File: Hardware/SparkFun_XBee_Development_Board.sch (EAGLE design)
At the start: 71 parts, among them J1 USB Female Type C Connector, J3 USB Female Type C Connector, J4 QWIIC_RIGHT_ANGLE, Q2 3.1A/30V/105mΩ, U1 FSUSB30MUX_MSOP10, U2 AP63203, U3 ESD Diode, U5 ESD Diode, U7 FT231XS

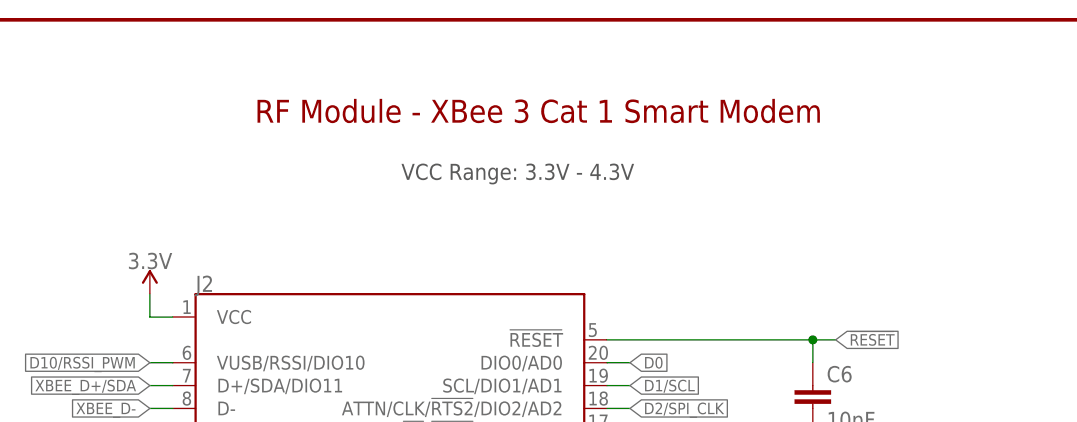
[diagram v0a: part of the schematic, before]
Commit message: Updates XBee section with correct name
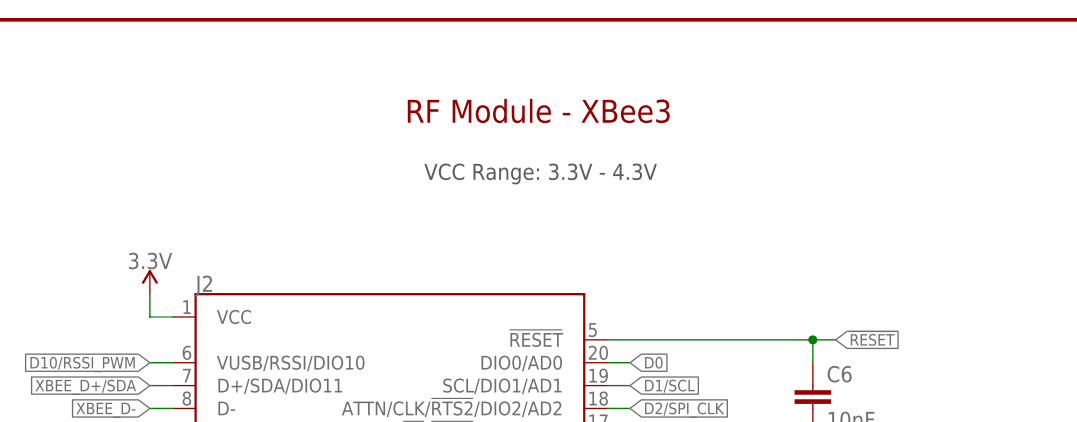
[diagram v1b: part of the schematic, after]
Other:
- note added: "RF Module - XBee3"
- note removed: "RF Module - XBee 3 Cat 1 Smart Modem"
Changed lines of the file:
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@@
 <sheet>
 <plain>
-<text x="45.72" y="261.62" size="1.778" layer="97" font="vector">VCC Range: 3.3V - 4.3V</text>
+<text x="48.26" y="261.62" size="1.778" layer="97" font="vector">VCC Range: 3.3V - 4.3V</text>
 <text x="363.22" y="269.24" size="2.54" layer="94" font="vector" align="center">USB to UART Bridge  - FT231XS</text>
 <text x="203.454" y="197.866" size="2.54" layer="94" font="vector" align="center">Buck Converter - AP63203</text>
@@
 <text x="172.72" y="96.52" size="1.778" layer="97" font="vector" align="center">Cut I2C jumper to remove pullups.</text>
 <text x="274.32" y="96.52" size="1.778" layer="97" font="vector" align="center">Cut respective jumper to sever power to LED.</text>
-<text x="60.96" y="269.24" size="2.54" layer="94" font="vector" align="center">RF Module - XBee 3 Cat 1 Smart Modem</text>
+<text x="60.96" y="269.24" size="2.54" layer="94" font="vector" align="center">RF Module - XBee3</text>
 <wire x1="0" y1="187.96" x2="121.92" y2="187.96" width="0.2032" layer="97" style="longdash"/>
 <text x="60.96" y="180.34" size="2.54" layer="94" font="vector" align="center">0.1" Headers</text>

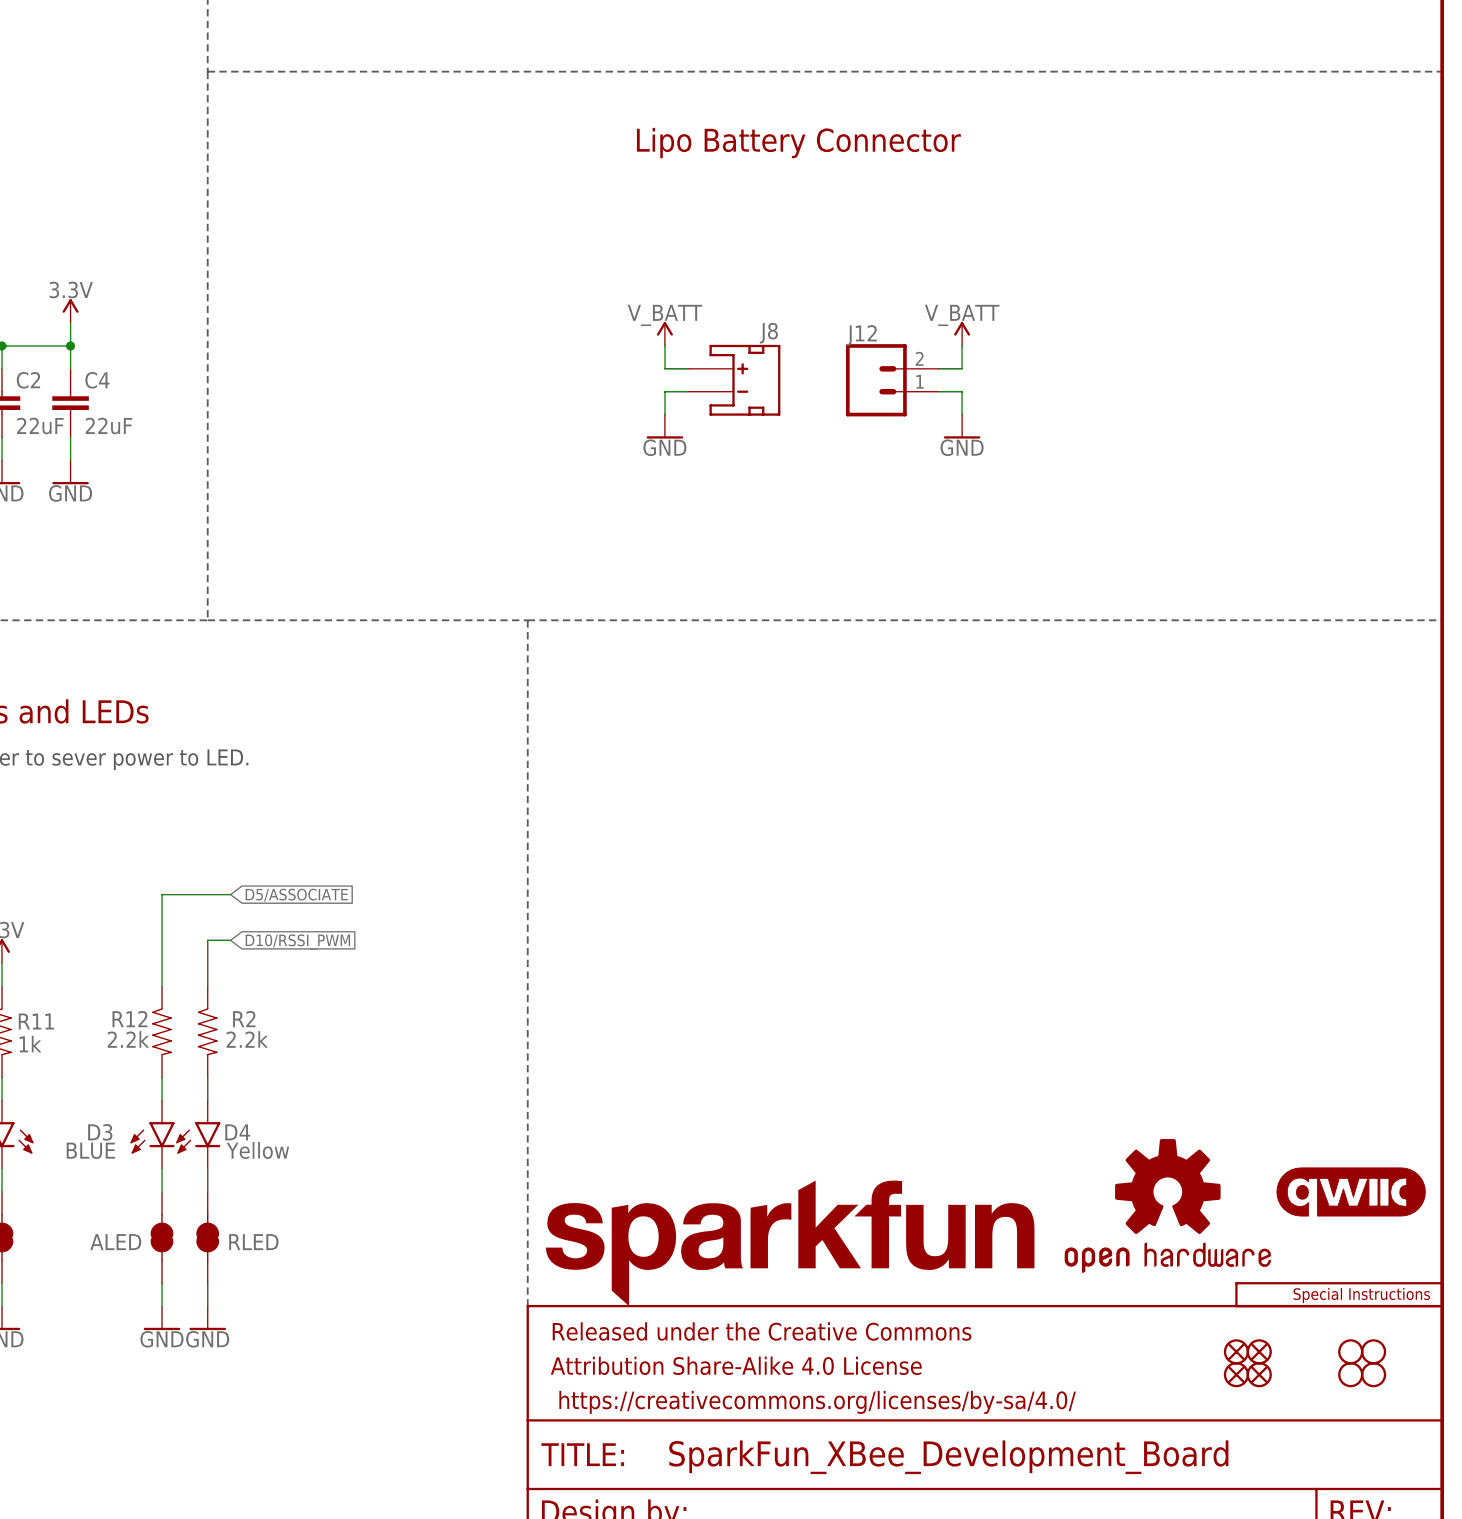
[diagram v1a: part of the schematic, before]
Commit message: Adds LED and Charging circuit - all routed (but not optimized
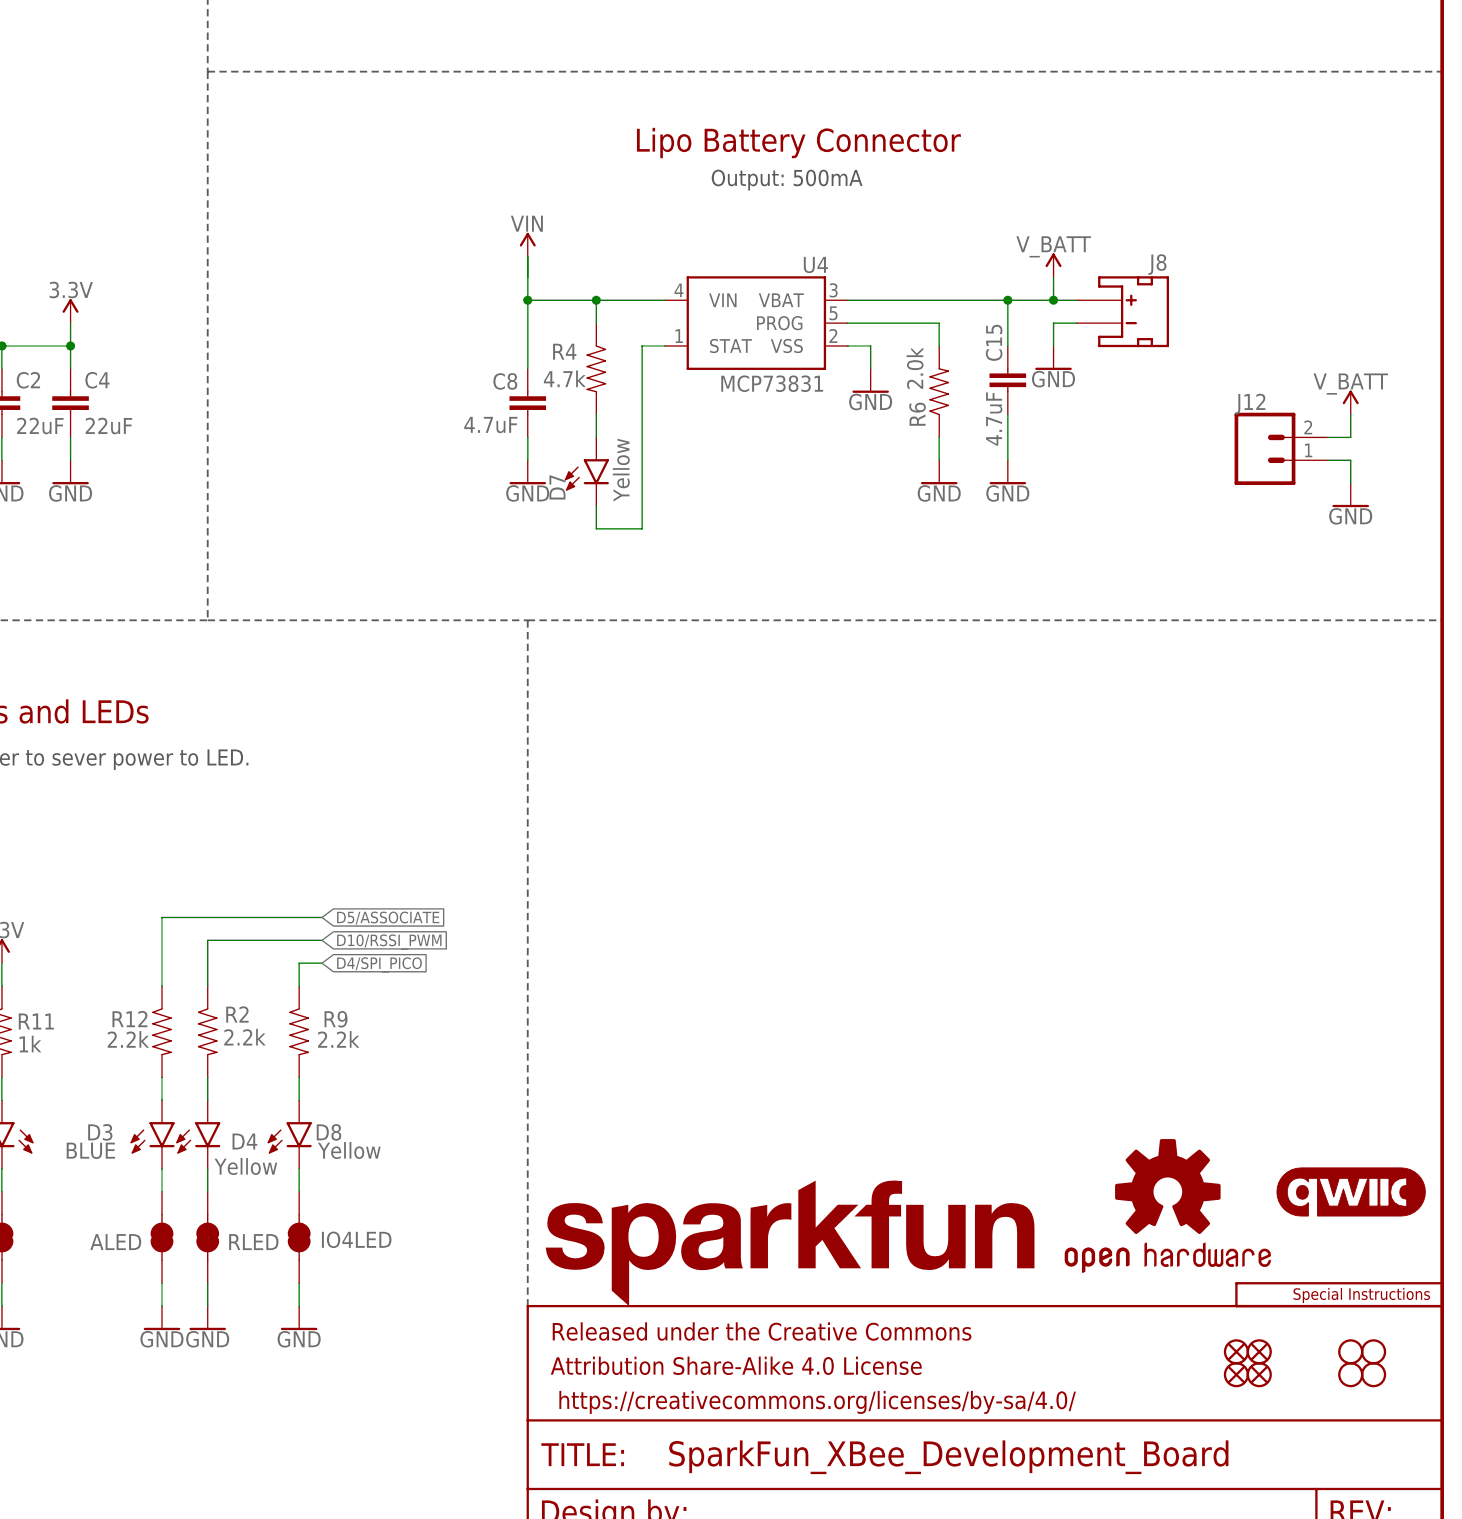
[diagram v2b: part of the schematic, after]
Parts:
- added C15: 4.7uF, SparkFun-Capacitors:4.7UF-0603-35V-(20%)
- added C8: 4.7uF, SparkFun-Capacitors:4.7UF-0603-6.3V-(10%)
- added D7, D8: Yellow, SparkFun-LED:LED-YELLOW0603
- added IO4LED: JUMPER-SMT_2_NC_TRACE_SILK, SparkFun-Jumpers:JUMPER-SMT_2_NC_TRACE_SILK
- added R4: 4.7k, SparkFun-Resistors:4.7KOHM-0603-1/10W-1%
- added R6: 2.0k, SparkFun-Resistors:2.0KOHM-0603-1/10W-5%
- added R9: 2.2k, SparkFun-Resistors:2.2KOHM-0603-1/10W-1%
- added U4: MCP73831, SparkFun-IC-Power:MCP73831
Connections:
- new net N$10: D7.A, R4.2
- new net N$17: D8.A, R9.2
- new net N$6: R6.2, U4.PROG
- new net N$9: D7.C, U4.STAT
- new net RLED1: D8.C, IO4LED.2
- net D4/SPI_PICO: now also R9.1
- net GND: now also C15.2, C8.2, IO4LED.1, R6.1, U4.VSS
- net VIN: now also C8.1, R4.1, U4.VIN
- net V_BATT: now also C15.1, U4.VBAT
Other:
- note added: "Output: 500mA"
- moved on the sheet: J12, J8

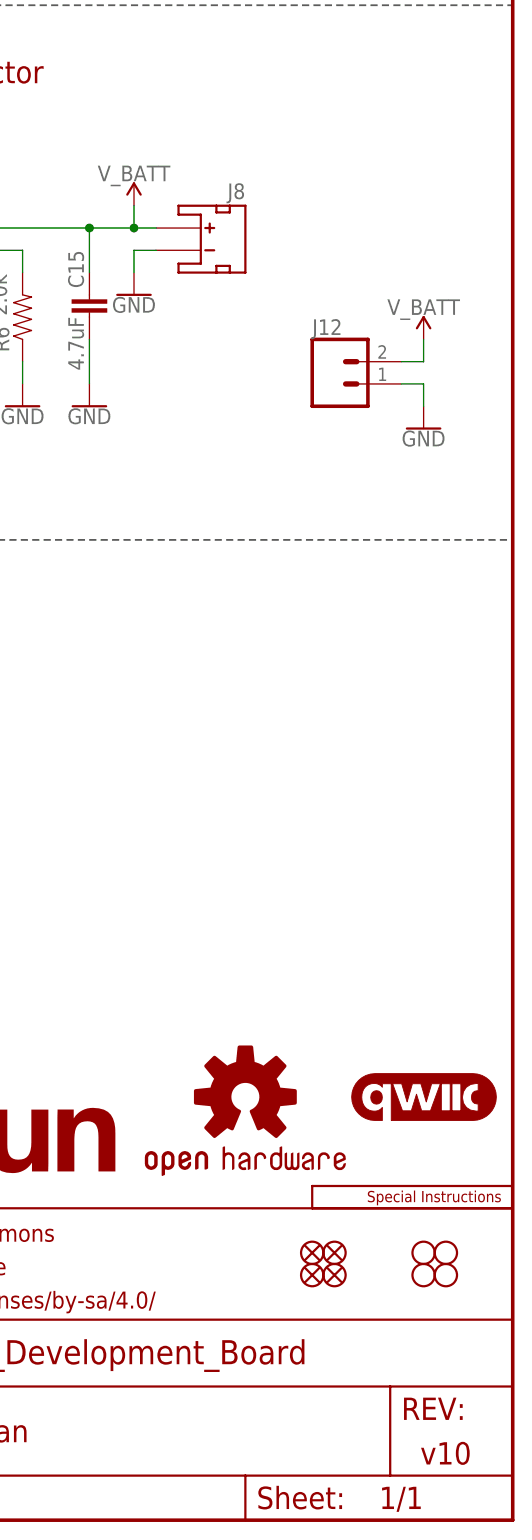
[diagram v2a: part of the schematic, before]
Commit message: Rolls version to v11 (applies to last commit)
* Adds silk
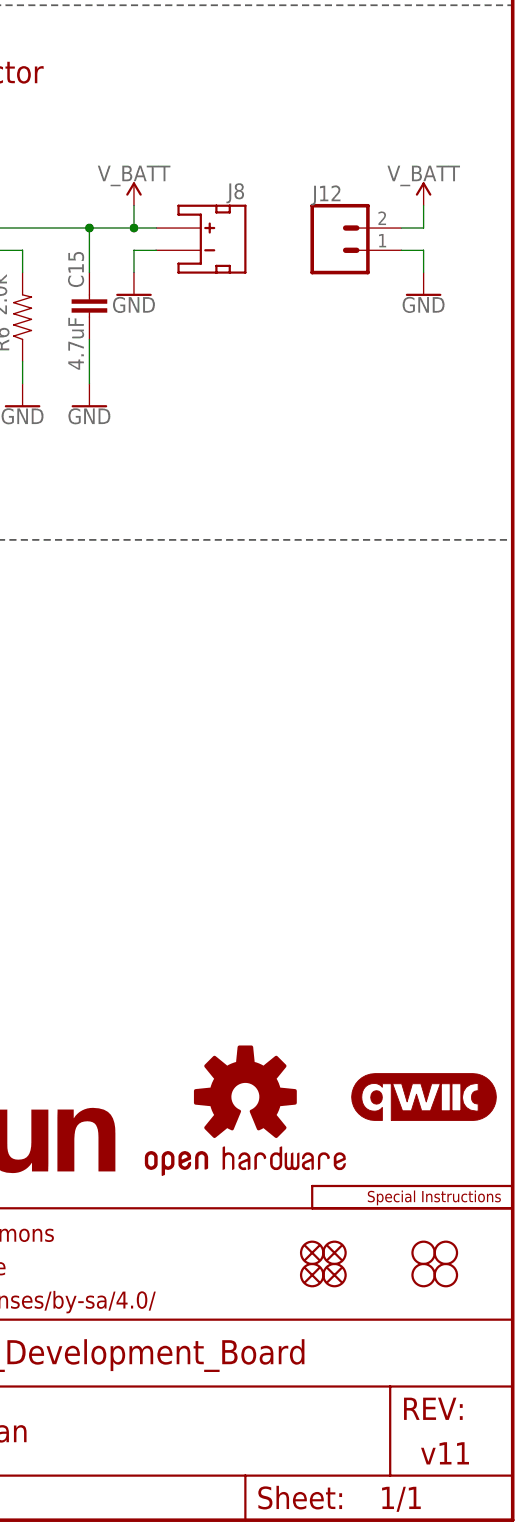
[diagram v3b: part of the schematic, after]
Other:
- note added: "v11"
- note removed: "v10"
- moved on the sheet: J12
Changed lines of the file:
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@@
 <part name="GND32" library="SparkFun-PowerSymbols" deviceset="GND" device=""/>
 <part name="SUPPLY22" library="SparkFun-PowerSymbols" deviceset="3.3V" device=""/>
-<part name="L1" library="SparkFun-Coils" deviceset="3.9UH" device=""/>
+<part name="L1" library="SparkFun-Coils" deviceset="3.9UH" device="" value="3.9UH"/>
 <part name="U4" library="SparkFun-IC-Power" deviceset="MCP73831" device=""/>
 <part name="R4" library="SparkFun-Resistors" deviceset="4.7KOHM" device="-0603-1/10W-1%" value="4.7k"/>
@@
 <wire x1="294.64" y1="172.72" x2="431.8" y2="172.72" width="0.2032" layer="97" style="longdash"/>
 <wire x1="121.92" y1="111.76" x2="121.92" y2="0" width="0.2032" layer="97" style="longdash"/>
-<text x="424.18" y="7.62" size="2.54" layer="94" font="vector" align="center">v10</text>
+<text x="424.18" y="7.62" size="2.54" layer="94" font="vector" align="center">v11</text>
 <text x="363.22" y="10.16" size="2.54" layer="94" font="vector" align="center">Elias Santistevan</text>
 <wire x1="223.52" y1="111.76" x2="223.52" y2="0" width="0.2032" layer="97" style="longdash"/>
@@
 <attribute name="VALUE" x="388.62" y="139.446" size="1.778" layer="96" font="vector" rot="MR0" align="top-center"/>
 </instance>
-<instance part="J12" gate="G$1" x="411.48" y="129.54" smashed="yes">
-<attribute name="VALUE" x="408.94" y="124.714" size="1.778" layer="96" font="vector"/>
-<attribute name="NAME" x="408.94" y="135.128" size="1.778" layer="95" font="vector"/>
-</instance>
-<instance part="GND5" gate="1" x="421.64" y="124.46" smashed="yes" rot="MR0">
-<attribute name="VALUE" x="421.64" y="124.206" size="1.778" layer="96" font="vector" rot="MR0" align="top-center"/>
-</instance>
-<instance part="SUPPLY3" gate="G$1" x="421.64" y="134.62" smashed="yes">
-<attribute name="VALUE" x="421.64" y="137.414" size="1.778" layer="96" font="vector" align="bottom-center"/>
+<instance part="J12" gate="G$1" x="411.48" y="144.78" smashed="yes">
+<attribute name="VALUE" x="408.94" y="139.954" size="1.778" layer="96" font="vector"/>
+<attribute name="NAME" x="408.94" y="150.368" size="1.778" layer="95" font="vector"/>
+</instance>
+<instance part="GND5" gate="1" x="421.64" y="139.7" smashed="yes" rot="MR0">
+<attribute name="VALUE" x="421.64" y="139.446" size="1.778" layer="96" font="vector" rot="MR0" align="top-center"/>
+</instance>
+<instance part="SUPPLY3" gate="G$1" x="421.64" y="149.86" smashed="yes">
+<attribute name="VALUE" x="421.64" y="152.654" size="1.778" layer="96" font="vector" align="bottom-center"/>
 </instance>
 <instance part="J4" gate="G$1" x="193.04" y="55.88" smashed="yes">
@@
 <segment>
 <pinref part="J12" gate="G$1" pin="1"/>
-<wire x1="419.1" y1="129.54" x2="421.64" y2="129.54" width="0.1524" layer="91"/>
-<wire x1="421.64" y1="129.54" x2="421.64" y2="127" width="0.1524" layer="91"/>
+<wire x1="419.1" y1="144.78" x2="421.64" y2="144.78" width="0.1524" layer="91"/>
+<wire x1="421.64" y1="144.78" x2="421.64" y2="142.24" width="0.1524" layer="91"/>
 <pinref part="GND5" gate="1" pin="GND"/>
 </segment>
@@
 <segment>
 <pinref part="J12" gate="G$1" pin="2"/>
-<wire x1="419.1" y1="132.08" x2="421.64" y2="132.08" width="0.1524" layer="91"/>
-<wire x1="421.64" y1="132.08" x2="421.64" y2="134.62" width="0.1524" layer="91"/>
+<wire x1="419.1" y1="147.32" x2="421.64" y2="147.32" width="0.1524" layer="91"/>
+<wire x1="421.64" y1="147.32" x2="421.64" y2="149.86" width="0.1524" layer="91"/>
 <pinref part="SUPPLY3" gate="G$1" pin="V_BATT"/>
 </segment>
